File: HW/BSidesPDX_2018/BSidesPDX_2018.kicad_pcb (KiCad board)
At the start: 2 copper layers, 94.7 x 67.7 mm, 45 parts, among them J1 AVR-ISP-6, J2 USB_B_Micro, U1 ATTINY861-15XD, X1 Badgelife_shitty_connector, X2 Badgelife_shitty_connector, X3 Badgelife_shitty_connector, X4 Badgelife_shitty_connector

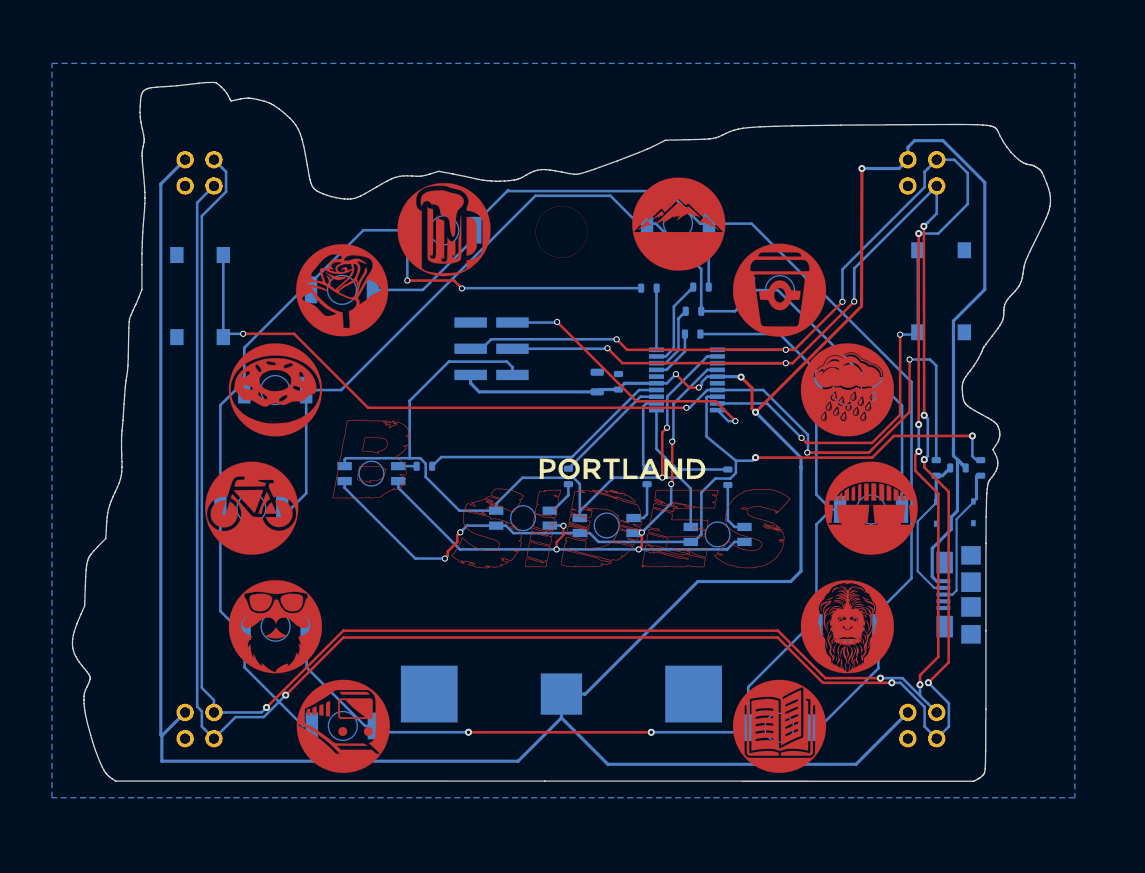
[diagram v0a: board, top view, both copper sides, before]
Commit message: fixing drc issues
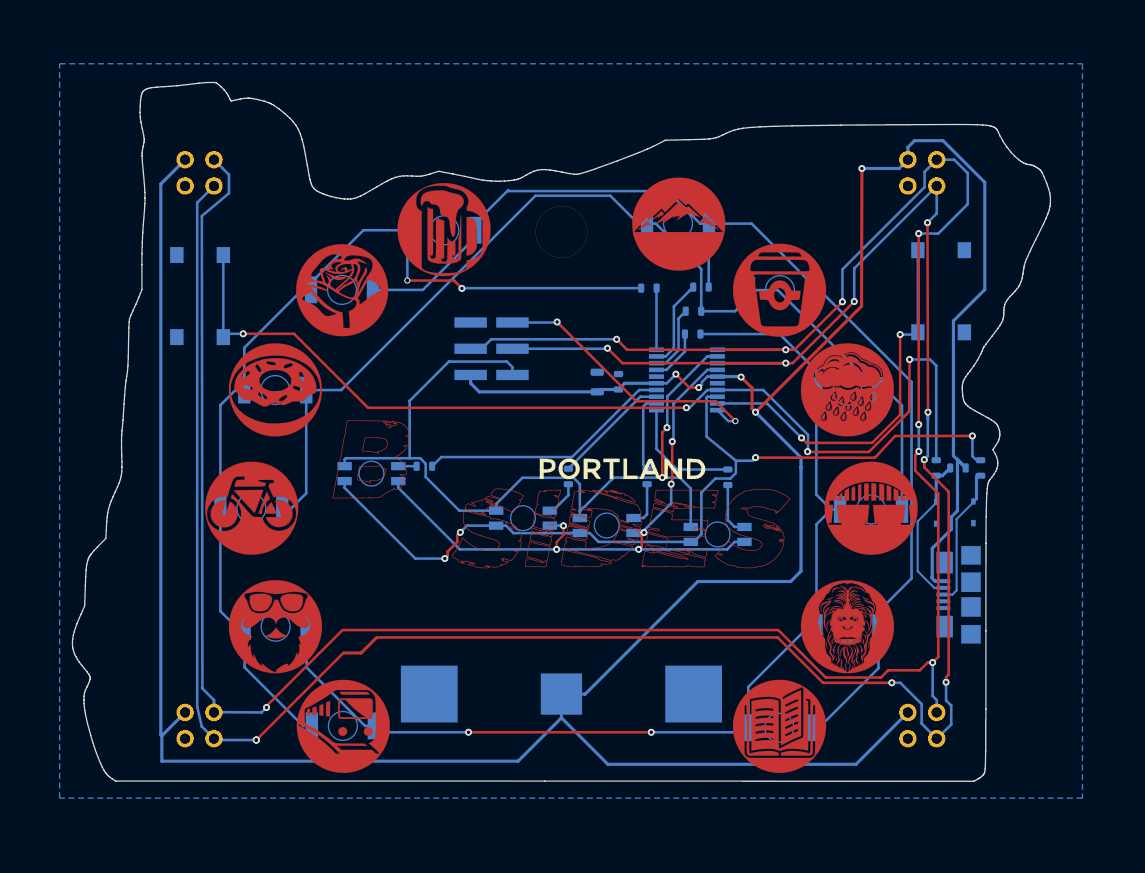
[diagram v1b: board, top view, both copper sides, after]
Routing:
- net /SCL_SCK: track 248.9 -> 247.9 mm, vias 9 -> 10
- net /SDA_MOSI: track 254.0 -> 254.3 mm, vias 9 -> 8

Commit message: fixing drc issues, now 40
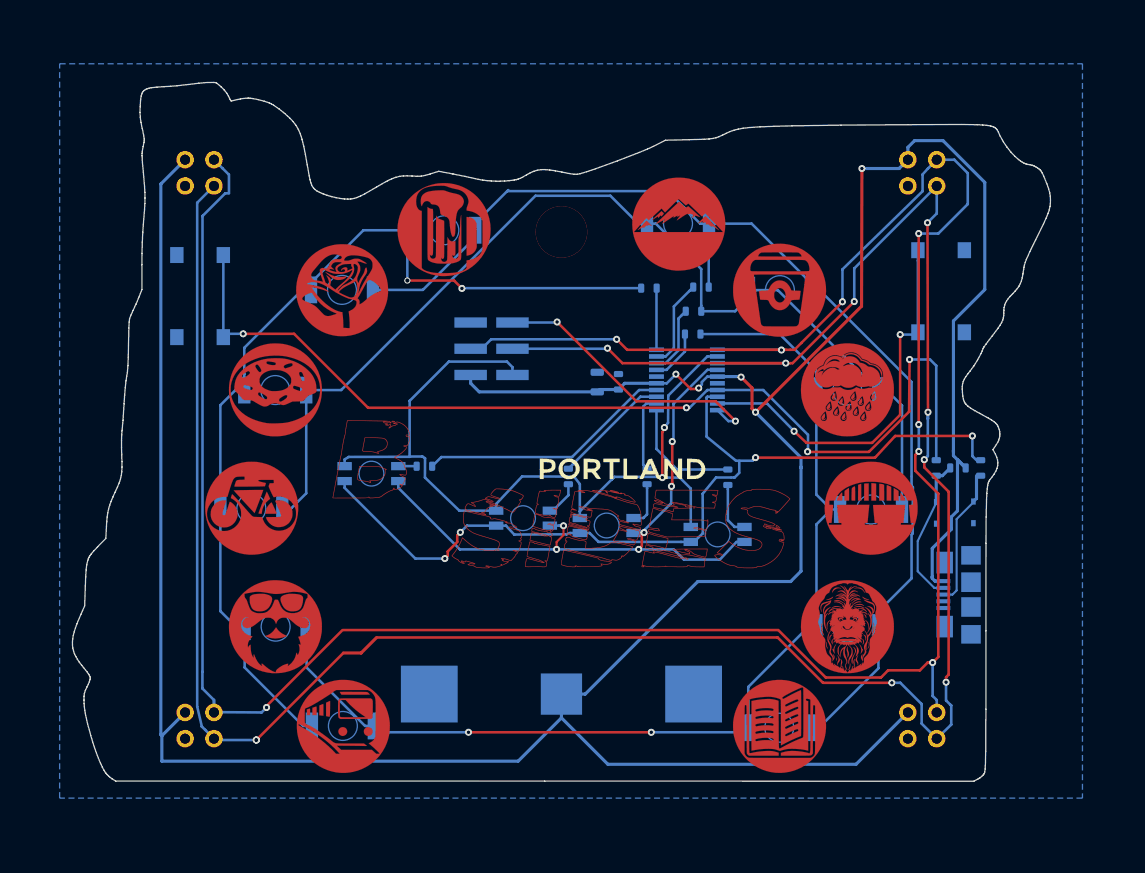
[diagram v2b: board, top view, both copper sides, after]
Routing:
- net /G_PWM: track 62.8 -> 63.6 mm

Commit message: filled in lower B with copper, layout looks googd
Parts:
- moved R4 0.63 mm to (161.7, 97.3)
- moved D101 0.16 mm to (130.2, 110.8)
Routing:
- net /ROW_3: track 102.1 -> 104.0 mm
- net /SDA_MOSI: track 253.9 -> 255.8 mm
- net /ROW_4: track 101.7 -> 101.1 mm
- net GND: vias 0 -> 4
- added copper zone on F.Cu, net GND
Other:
- net class Default: clearance 0.254 -> 0.1524; trace_width 0.254 -> 0.1524
- rule pad_to_mask_clearance: 0.2 -> 0.0508
- rule trace_clearance: 0.254 -> 0.1524

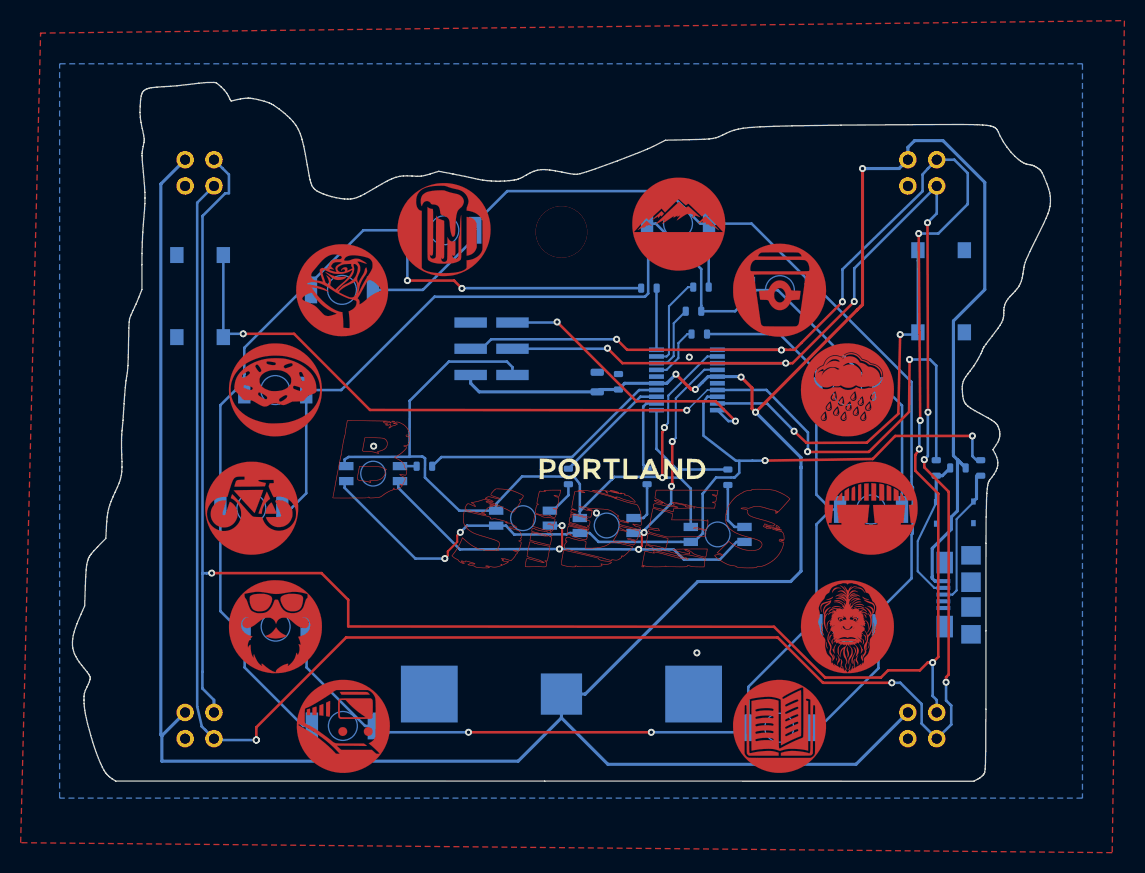
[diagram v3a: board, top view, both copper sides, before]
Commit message: fixed up ground connections, Added bottom silks
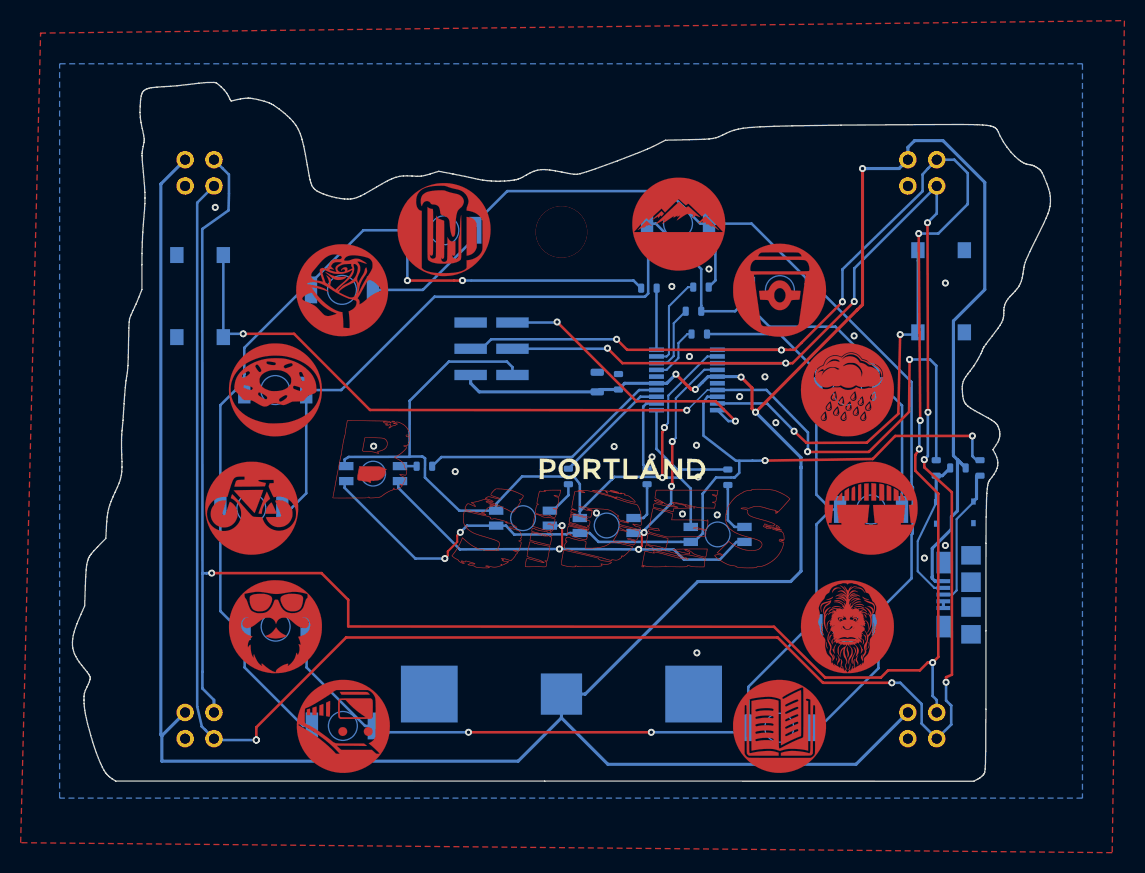
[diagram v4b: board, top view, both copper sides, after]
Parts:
- added G***: LOGO, BSidesPDX_2018:B.Silk, F.Cu at (83.7, 111.3)
- moved R5 0.06 mm to (188.9, 110.3)
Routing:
- net /ROW_3: track 104.0 -> 106.1 mm
- net GND: track 0.00 -> 0.65 mm, vias 4 -> 21
- net /ROW_2: track 109.3 -> 109.8 mm
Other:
- board text added: "@offic_deskjet"
- board text added: "@securelyfitz"
- board text added: "Design by:"
- board text added: "Remove battery to use USB"

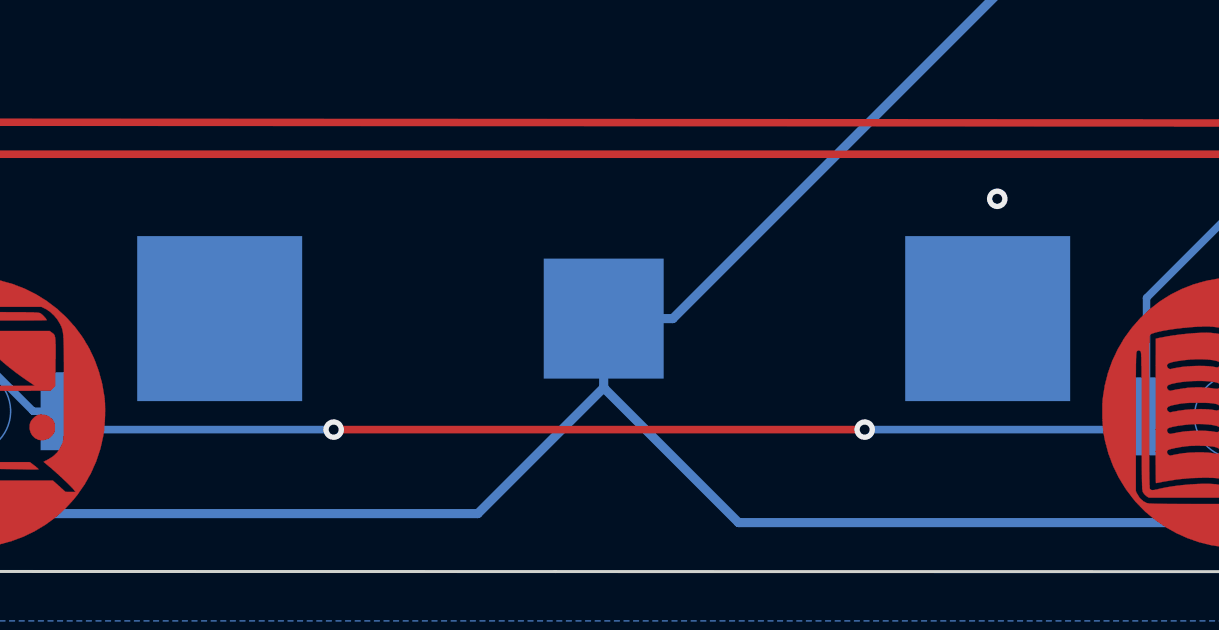
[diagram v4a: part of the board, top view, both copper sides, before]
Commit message: tying some vias through gnd to give physical attachmentwq
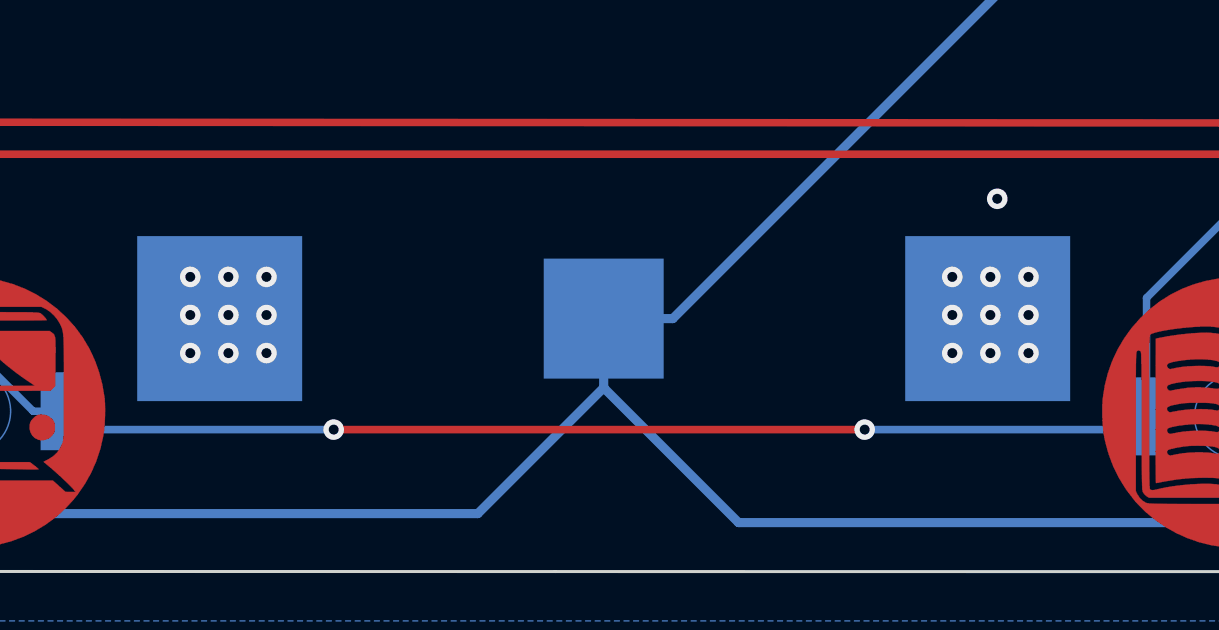
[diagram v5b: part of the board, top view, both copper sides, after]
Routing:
- net GND: vias 21 -> 39
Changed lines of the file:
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@@
-(kicad_pcb (version 20171130) (host pcbnew 5.0.0-fee4fd1~66~ubuntu16.04.1)
+(kicad_pcb (version 20171130) (host pcbnew 5.0.0-fee4fd1~66~ubuntu18.04.1)
   (general
     (thickness 1.6)
     (drawings 412)
-    (tracks 545)
+    (tracks 563)
     (zones 0)
     (modules 46)
@@
   (page A4)
   (layers
-    (0 F.Cu signal hide)
+    (0 F.Cu signal)
     (31 B.Cu signal)
     (32 B.Adhes user)
@@
     (37 F.SilkS user)
     (38 B.Mask user)
-    (39 F.Mask user hide)
+    (39 F.Mask user)
     (40 Dwgs.User user)
     (41 Cmts.User user)
@@
     (46 B.CrtYd user)
     (47 F.CrtYd user)
-    (48 B.Fab user hide)
+    (48 B.Fab user)
     (49 F.Fab user)
   )
   (setup
-    (last_trace_width 0.3048)
+    (last_trace_width 0.1524)
     (user_trace_width 0.2032)
     (user_trace_width 0.254)
@@
   (gr_line (start 105.2223 140.626838) (end 104.86883 140.394038) (layer Edge.Cuts) (width 0.1))
   (gr_line (start 104.86883 140.394038) (end 104.86699 140.393868) (layer Edge.Cuts) (width 0.1))
+  (via (at 137.16 133.35) (size 0.6858) (drill 0.3302) (layers F.Cu B.Cu) (net 1))
+  (via (at 135.89 133.35) (size 0.6858) (drill 0.3302) (layers F.Cu B.Cu) (net 1))
+  (via (at 134.62 133.35) (size 0.6858) (drill 0.3302) (layers F.Cu B.Cu) (net 1))
+  (via (at 134.62 132.08) (size 0.6858) (drill 0.3302) (layers F.Cu B.Cu) (net 1))
+  (via (at 134.62 130.81) (size 0.6858) (drill 0.3302) (layers F.Cu B.Cu) (net 1))
+  (via (at 135.89 130.81) (size 0.6858) (drill 0.3302) (layers F.Cu B.Cu) (net 1))
+  (via (at 137.16 130.81) (size 0.6858) (drill 0.3302) (layers F.Cu B.Cu) (net 1))
+  (via (at 137.16 132.08) (size 0.6858) (drill 0.3302) (layers F.Cu B.Cu) (net 1))
+  (via (at 135.89 132.08) (size 0.6858) (drill 0.3302) (layers F.Cu B.Cu) (net 1))
+  (via (at 161.29 132.08) (size 0.6858) (drill 0.3302) (layers F.Cu B.Cu) (net 1))
+  (via (at 160.02 132.08) (size 0.6858) (drill 0.3302) (layers F.Cu B.Cu) (net 1))
+  (via (at 160.02 133.35) (size 0.6858) (drill 0.3302) (layers F.Cu B.Cu) (net 1))
+  (via (at 161.29 133.35) (size 0.6858) (drill 0.3302) (layers F.Cu B.Cu) (net 1))
+  (via (at 162.56 133.35) (size 0.6858) (drill 0.3302) (layers F.Cu B.Cu) (net 1))
+  (via (at 162.56 132.08) (size 0.6858) (drill 0.3302) (layers F.Cu B.Cu) (net 1))
+  (via (at 162.56 130.81) (size 0.6858) (drill 0.3302) (layers F.Cu B.Cu) (net 1))
+  (via (at 161.29 130.81) (size 0.6858) (drill 0.3302) (layers F.Cu B.Cu) (net 1))
+  (via (at 160.02 130.81) (size 0.6858) (drill 0.3302) (layers F.Cu B.Cu) (net 1))
   (via (at 161.5186 128.2065) (size 0.6858) (drill 0.3302) (layers F.Cu B.Cu) (net 1))
   (via (at 160.7947 99.5045) (size 0.6858) (drill 0.3302) (layers F.Cu B.Cu) (net 1))

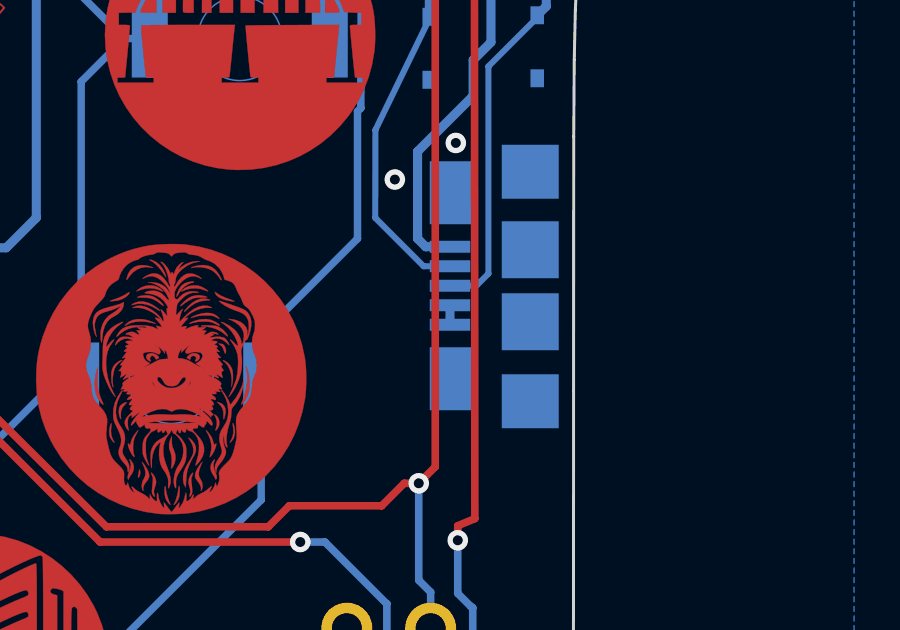
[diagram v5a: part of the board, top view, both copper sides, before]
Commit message: Updated BOM, disconnected USB ID Pin
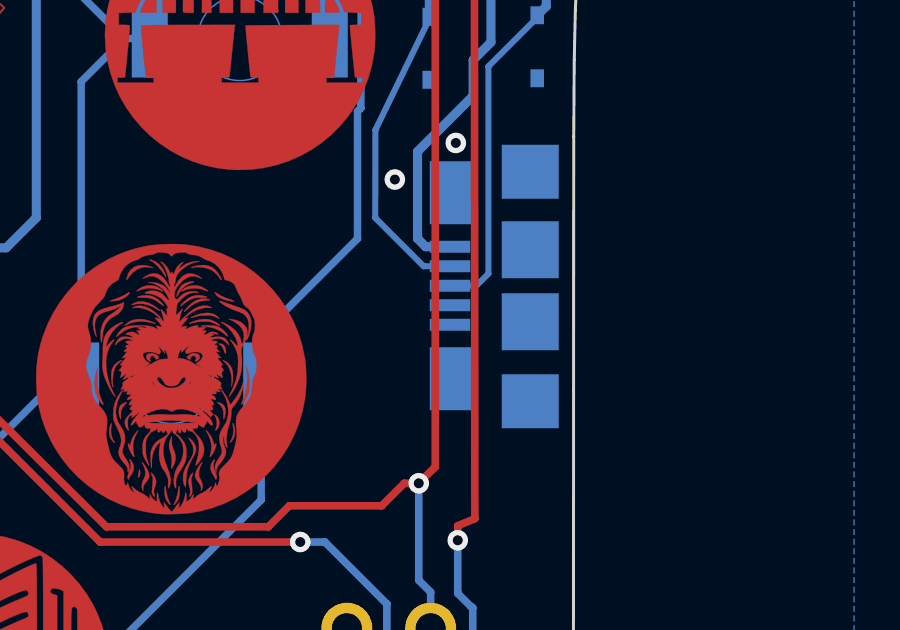
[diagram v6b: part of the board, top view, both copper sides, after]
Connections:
- J2 pad 4: GND -> /NC
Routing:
- net GND: track 0.65 -> 0.00 mm
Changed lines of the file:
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@@
-(kicad_pcb (version 20171130) (host pcbnew 5.0.0-fee4fd1~66~ubuntu18.04.1)
+(kicad_pcb (version 20171130) (host pcbnew 5.0.0-4.fc30)
   (general
     (thickness 1.6)
     (drawings 412)
-    (tracks 563)
+    (tracks 562)
     (zones 0)
     (modules 46)
-    (nets 29)
+    (nets 30)
   )
   (page A4)
@@
   (net 27 /SDA_MOSI)
   (net 28 /L_SWITCH_D-)
+  (net 29 /NC)
   (net_class Default "This is the default net class."
     (clearance 0.1524)
@@
     (add_net /G_PWM)
     (add_net /L_SWITCH_D-)
+    (add_net /NC)
     (add_net /ROW1)
     (add_net /ROW2)
@@
       (net 1 GND))
     (pad 4 smd rect (at 0.65 2.675 270) (size 0.4 1.35) (layers B.Cu B.Paste B.Mask)
-      (net 1 GND))
+      (net 29 /NC))
     (pad 3 smd rect (at 0 2.675 270) (size 0.4 1.35) (layers B.Cu B.Paste B.Mask)
       (net 23 /D+))
@@
   (via (at 168.1099 101.473) (size 0.6858) (drill 0.3302) (layers F.Cu B.Cu) (net 1))
   (via (at 160.1216 114.7572) (size 0.6858) (drill 0.3302) (layers F.Cu B.Cu) (net 1))
-  (segment (start 185.39168 123.86516) (end 185.39168 123.21516) (width 0.3048) (layer B.Cu) (net 1))
   (segment (start 154.5268 102.1028) (end 153.924 102.7056) (width 0.3048) (layer B.Cu) (net 2))
   (segment (start 157.6034 102.1028) (end 154.5268 102.1028) (width 0.3048) (layer B.Cu) (net 2))
